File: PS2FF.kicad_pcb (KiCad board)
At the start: 2 copper layers, 38.1 x 74.7 mm, 11 parts, among them J1 PS2_SIDE, J2 DATA_RATE, J3 FF_SIDE, J4 POWER, SW1 DRIVE_TYPE, SW2 MEDIA_TYPE

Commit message: Fix up some DRC errors in the schematic
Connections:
- J3 pad 2: /~{FF_O_DENSITY} -> unconnected-(J3-Pad2)
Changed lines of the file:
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@@
   (net 22 "/DATA_RATE_0")
   (net 23 "/~{DISKETTE_CHANGE}")
-  (net 24 "/~{FF_O_DENSITY}")
+  (net 24 "unconnected-(J3-Pad2)")
   (net 25 "/~{FF_I_DS1}")
   (footprint "Connector_IDC:IDC-Header_2x17_P2.54mm_Horizontal" (layer "F.Cu")
@@
       (net 3 "GND") (pinfunction "Pin_1") (pintype "passive"))
     (pad "2" thru_hole circle (at 2.54 0) (size 1.7 1.7) (drill 1) (layers *.Cu *.Mask)
-      (net 24 "/~{FF_O_DENSITY}") (pinfunction "Pin_2") (pintype "passive+no_connect"))
+      (net 24 "unconnected-(J3-Pad2)") (pinfunction "Pin_2") (pintype "passive+no_connect"))
     (pad "3" thru_hole circle (at 0 -2.54) (size 1.7 1.7) (drill 1) (layers *.Cu *.Mask)
       (net 3 "GND") (pinfunction "Pin_3") (pintype "passive"))

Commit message: Bump the board rev since new changes
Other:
- board text added: "PS2FF Media Sense Adapter June Tate-Gans june@theonelab.com CC-BY-SA Board Rev B Schematic Rev B"
- board text removed: "PS2FF Media Sense Adapter June Tate-Gans june@theonelab.com CC-BY-SA Board Rev A Schematic Rev A"
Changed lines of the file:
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@@
     (effects (font (size 1 1) (thickness 0.15)) (justify left))
   )
-  (gr_text "PS2FF Media Sense Adapter\nJune Tate-Gans\njune@theonelab.com\nCC-BY-SA\nBoard Rev A\nSchematic Rev A" (at 110.998 60.833) (layer "F.SilkS")
+  (gr_text "PS2FF Media Sense Adapter\nJune Tate-Gans\njune@theonelab.com\nCC-BY-SA\nBoard Rev B\nSchematic Rev B" (at 110.998 60.833) (layer "F.SilkS")
     (effects (font (size 1 1) (thickness 0.15)) (justify left))
   )

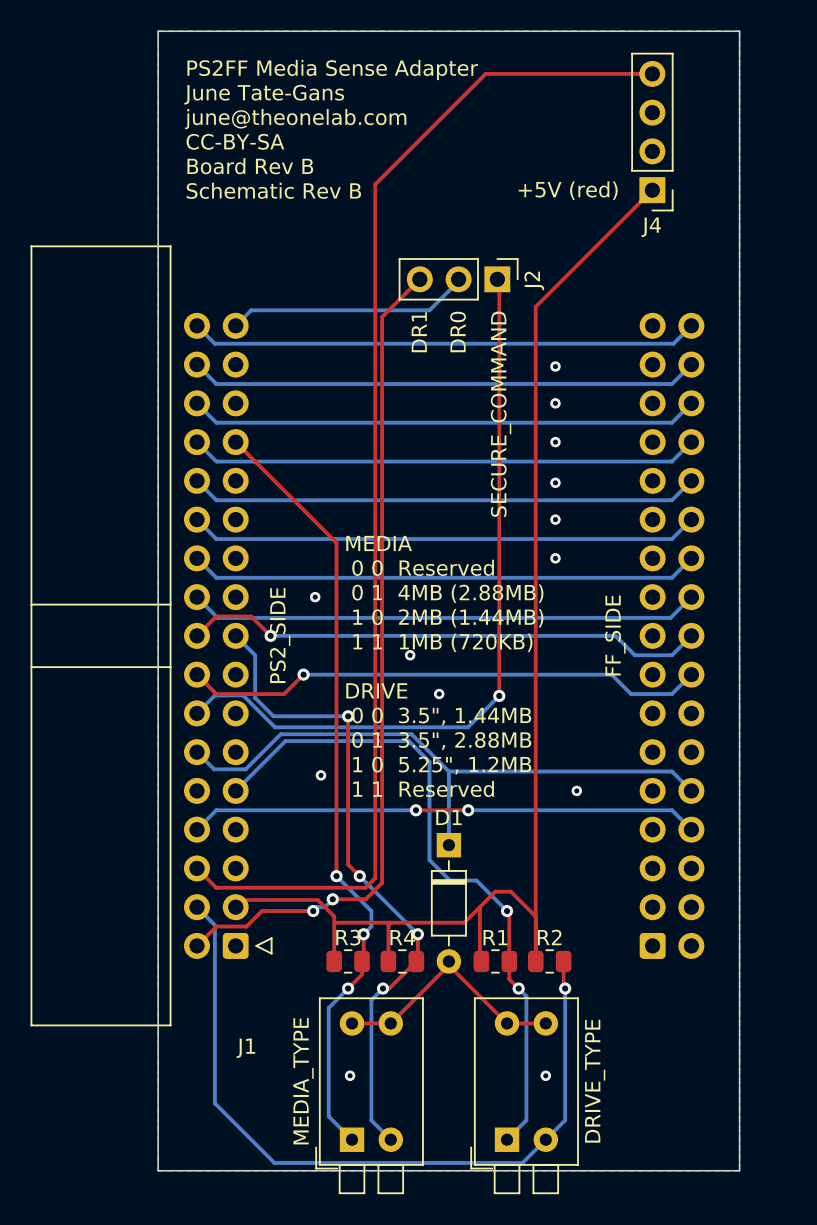
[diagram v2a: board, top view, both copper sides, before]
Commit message: automate things: Swap to using a buffer to automate
  - Use a simple buffer to drive outputs to the host side.
  - Wire in FF_O_DENSITY to the appropriate pin via the buffers.
    Note: this requires FF to be set to invert this output!
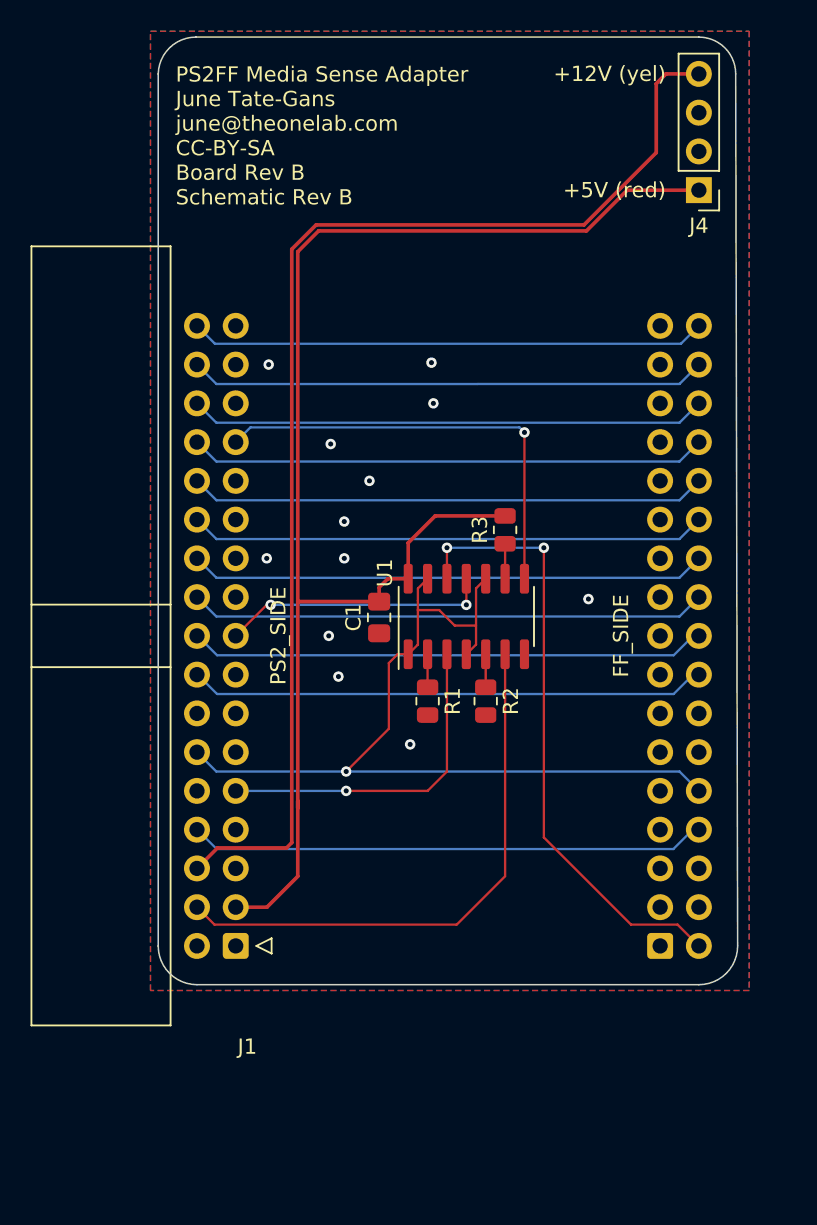
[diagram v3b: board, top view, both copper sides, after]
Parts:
- removed D1: 1N914, Diode_THT:D_DO-35_SOD27_P7.62mm_Horizontal
- removed J2: DATA_RATE, Connector_PinHeader_2.54mm:PinHeader_1x03_P2.54mm_Vertical
- removed R4: 1K, Resistor_SMD:R_0805_2012Metric
- removed SW1: DRIVE_TYPE, Button_Switch_THT:SW_DIP_SPSTx02_Piano_10.8x6.64mm_W7.62mm_P2.54mm
- removed SW2: MEDIA_TYPE, Button_Switch_THT:SW_DIP_SPSTx02_Piano_10.8x6.64mm_W7.62mm_P2.54mm
- added C1: 10pF, Capacitor_SMD:C_0805_2012Metric_Pad1.18x1.45mm_HandSolder, F.Cu at (123.7, 92.8)
- added U1: 74LS125, Package_SO:SOIC-14_3.9x8.7mm_P1.27mm, F.Cu at (129.4, 92.7)
- moved R3 30.1 mm to (132.0, 87.0), turned to 90 degrees
- moved R1 17.6 mm to (126.9, 98.3), turned to -90 degrees
- moved R2 17.6 mm to (130.7, 98.3), turned to -90 degrees
- moved J4 3.05 mm to (144.7, 64.8)
- moved J3 0.49 mm to (142.1, 114.3)
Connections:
- J3 pad 2: unconnected-(J3-Pad2) -> /~{FF_O_DENSITY}
- R1 pad 1: /DRIVE0_STATUS0 -> Net-(R1-Pad1)
- R1 pad 2: +5V -> GND
- R2 pad 1: /DRIVE1_STATUS1 -> Net-(R2-Pad1)
- R2 pad 2: +5V -> GND
- R3 pad 1: /MEDIA0_STATUS2 -> Net-(U1-Pad9)
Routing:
- net /DATA_RATE_1: track 54.4 -> 0.00 mm, vias 2 -> 0
- net /~{SECURITY_COMMAND}: track 49.4 -> 0.00 mm, vias 1 -> 0
- net /~{FF_O_DENSITY}: track 0.00 -> 40.5 mm, vias 0 -> 2
- net /MEDIA1_STATUS3: track 42.9 -> 17.7 mm, vias 4 -> 2
- net /MEDIA0_STATUS2: track 51.2 -> 29.0 mm, vias 3 -> 1
- net /DRIVE0_STATUS0: track 43.6 -> 22.1 mm, vias 2 -> 1
- net /~{DRIVE_SELECT}: track 40.2 -> 58.9 mm, vias 0 -> 1
- net Net-(D1-Pad2): track 16.1 -> 0.00 mm
- net /DATA_RATE_0: track 15.9 -> 0.00 mm
- net /DRIVE1_STATUS1: track 49.5 -> 36.5 mm, vias 1 -> 0
- net +5V: track 87.5 -> 92.2 mm
- net Net-(U1-Pad9): track 0.00 -> 2.29 mm
- net Net-(R2-Pad1): track 0.00 -> 2.16 mm
- net Net-(R1-Pad1): track 0.00 -> 2.16 mm
- net /~{FF_I_MO}: track 34.5 -> 33.4 mm, vias 1 -> 0
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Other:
- board size 38.1 x 74.7 mm -> 38 x 62.1 mm
- board text added: "+12V (yel)"
- board text removed: "DR0"
- board text removed: "DR1"
- board text removed: "MEDIA 0 0 Reserved 0 1 4MB (2.88MB) 1 0 2MB (1.44MB) 1 1 1MB (720KB) DRIVE 0 0 3.5{dblquote}, 1.44MB 0 1 3.5{dblquote}, 2.88MB 1 0 5.25{dblquote}, 1.2MB 1 1 Reserved"
- board text removed: "SECURE_COMMAND"

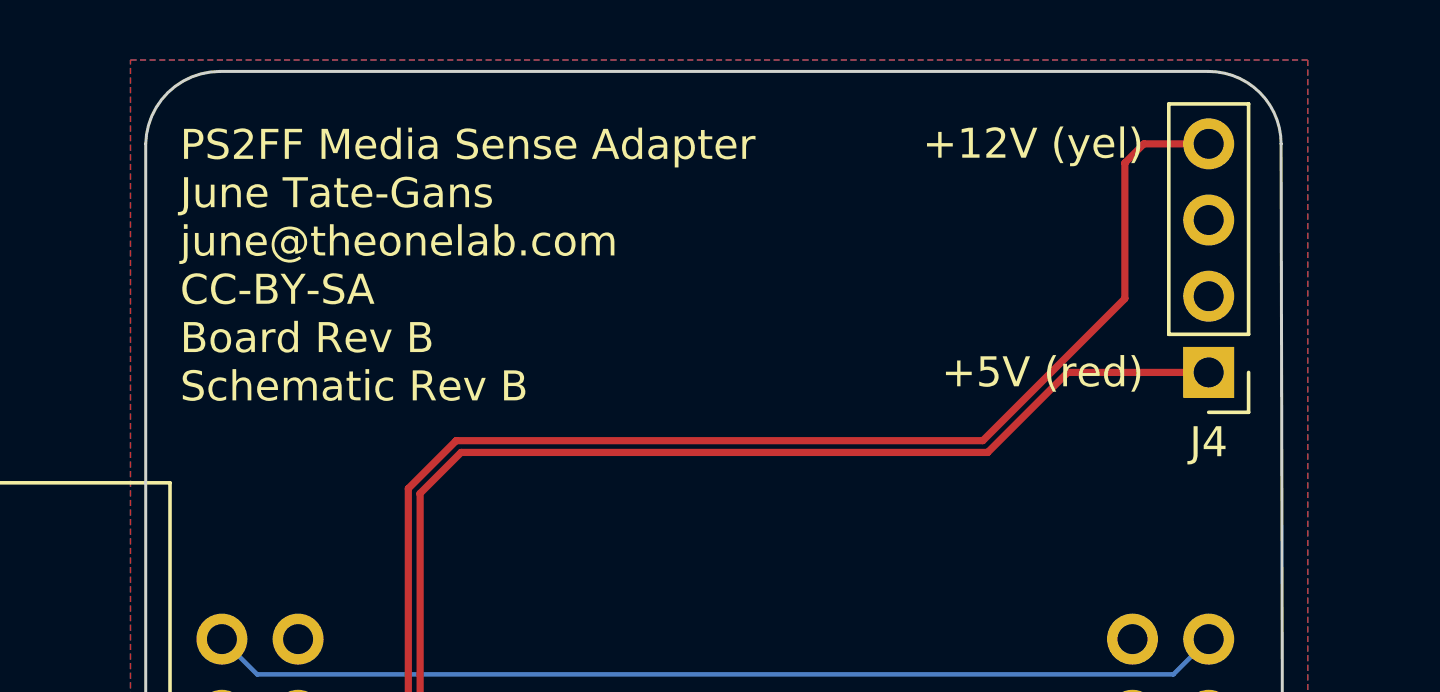
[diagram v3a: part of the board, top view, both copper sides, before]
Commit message: silks: Add a note about the hdout pin
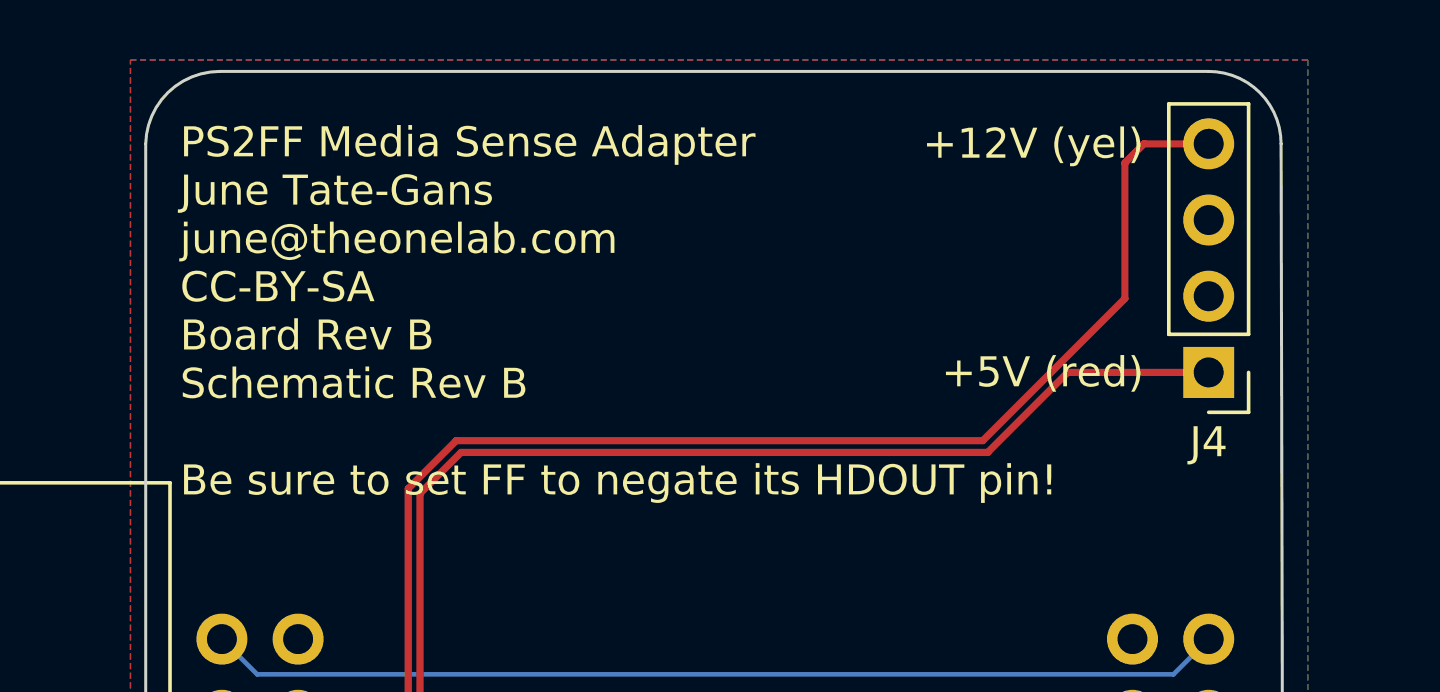
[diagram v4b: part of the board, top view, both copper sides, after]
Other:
- board text added: "PS2FF Media Sense Adapter June Tate-Gans june@theonelab.com CC-BY-SA Board Rev B Schematic Rev B Be sure to set FF to negate its HDOUT pin!"
- board text removed: "PS2FF Media Sense Adapter June Tate-Gans june@theonelab.com CC-BY-SA Board Rev B Schematic Rev B"
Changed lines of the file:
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@@
     (effects (font (size 1 1) (thickness 0.15)) (justify right))
   )
-  (gr_text "PS2FF Media Sense Adapter\nJune Tate-Gans\njune@theonelab.com\nCC-BY-SA\nBoard Rev B\nSchematic Rev B" (at 110.363 61.214) (layer "F.SilkS")
+  (gr_text "PS2FF Media Sense Adapter\nJune Tate-Gans\njune@theonelab.com\nCC-BY-SA\nBoard Rev B\nSchematic Rev B\n\nBe sure to set FF to negate its HDOUT pin!" (at 110.363 62.738) (layer "F.SilkS")
     (effects (font (size 1 1) (thickness 0.15)) (justify left))
   )

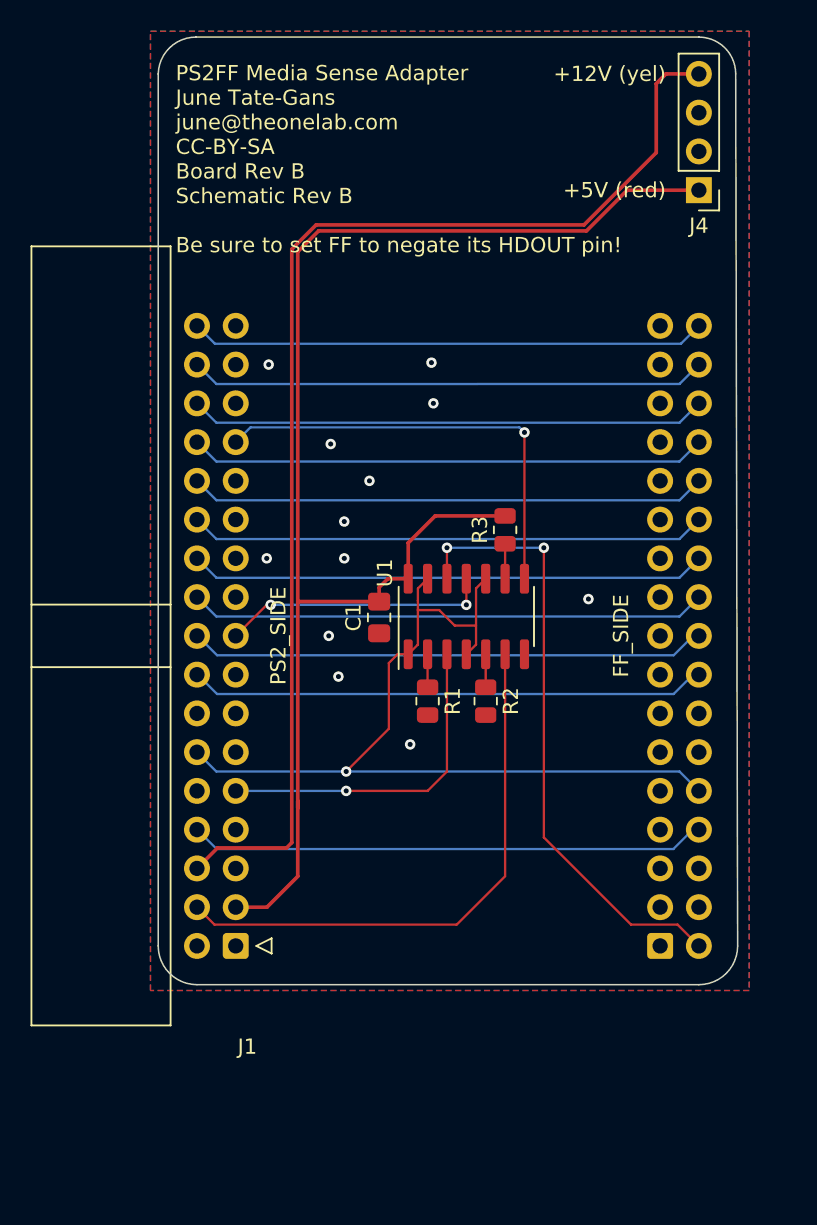
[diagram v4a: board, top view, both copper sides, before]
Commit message: writing: Actually wire up the HDOUT pin from the FF side
Update the links with the rev B schematic/PCB for fab.
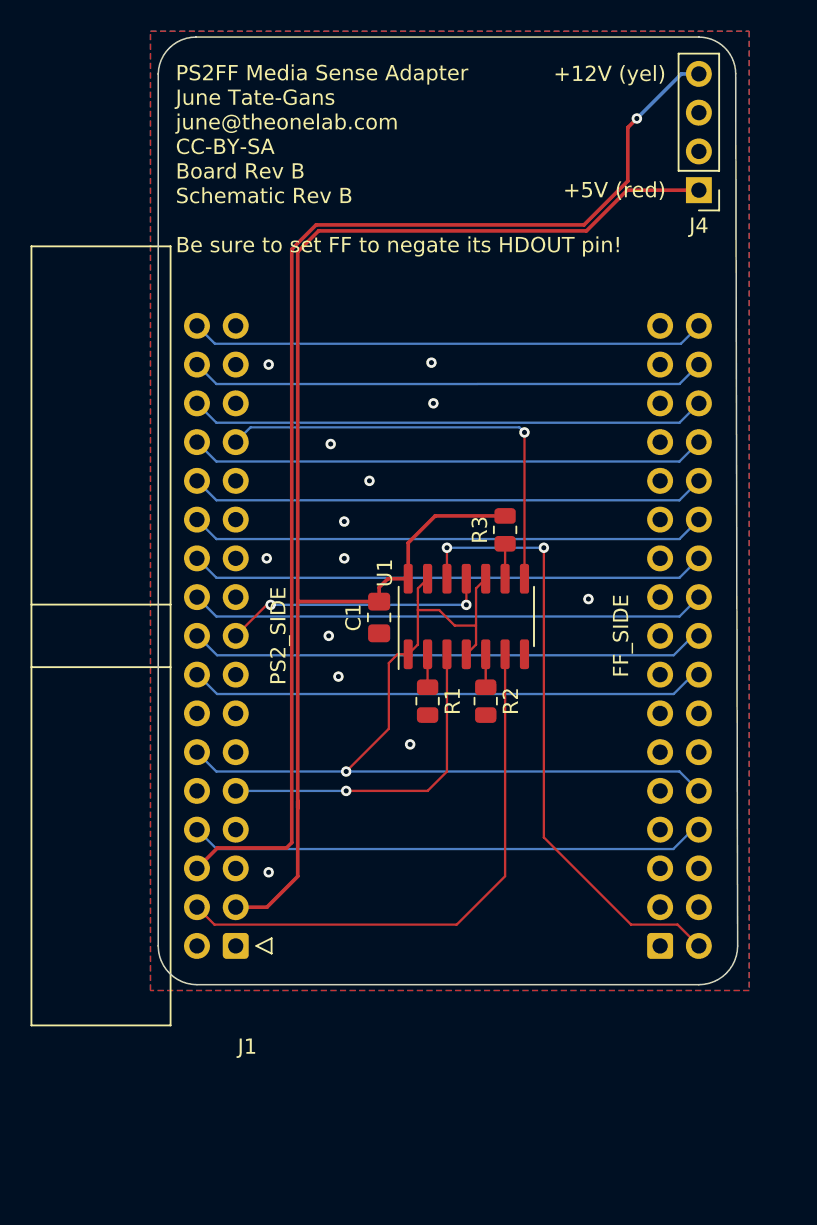
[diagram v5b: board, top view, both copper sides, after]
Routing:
- net +12V: track 79.9 -> 79.3 mm, vias 0 -> 1
- net GND: vias 12 -> 13
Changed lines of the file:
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@@
   (segment (start 121.539 102.87) (end 113.03 102.87) (width 0.1524) (layer "B.Cu") (net 1))
   (segment (start 113.03 102.87) (end 111.76 101.6) (width 0.1524) (layer "B.Cu") (net 1))
+  (via (at 116.459 109.474) (size 0.6858) (drill 0.3302) (layers "F.Cu" "B.Cu") (free) (net 2))
   (via (at 123.063 83.82) (size 0.6858) (drill 0.3302) (layers "F.Cu" "B.Cu") (free) (net 2))
   (via (at 127.254 78.74) (size 0.6858) (drill 0.3302) (layers "F.Cu" "B.Cu") (free) (net 2))
@@
   (segment (start 131.953 95.185) (end 131.953 109.728) (width 0.1524) (layer "F.Cu") (net 5))
   (segment (start 128.778 112.903) (end 112.903 112.903) (width 0.1524) (layer "F.Cu") (net 5))
-  (segment (start 113.103292 107.876708) (end 117.628354 107.876708) (width 0.24) (layer "F.Cu") (net 6))
-  (segment (start 117.9716 68.642715) (end 119.569715 67.0446) (width 0.24) (layer "F.Cu") (net 6))
-  (segment (start 117.628354 107.876708) (end 117.9716 107.533462) (width 0.24) (layer "F.Cu") (net 6))
-  (segment (start 111.76 109.22) (end 113.103292 107.876708) (width 0.24) (layer "F.Cu") (net 6))
-  (segment (start 142.494 57.15) (end 144.653 57.15) (width 0.24) (layer "F.Cu") (net 6))
-  (segment (start 141.859 62.310062) (end 141.859 57.785) (width 0.24) (layer "F.Cu") (net 6))
-  (segment (start 137.124462 67.0446) (end 141.859 62.310062) (width 0.24) (layer "F.Cu") (net 6))
-  (segment (start 119.569715 67.0446) (end 137.124462 67.0446) (width 0.24) (layer "F.Cu") (net 6))
-  (segment (start 117.9716 107.533462) (end 117.9716 68.642715) (width 0.24) (layer "F.Cu") (net 6))
-  (segment (start 141.859 57.785) (end 142.494 57.15) (width 0.24) (layer "F.Cu") (net 6))
+  (segment (start 117.9716 107.533462) (end 117.628354 107.876708) (width 0.24) (layer "F.Cu") (net 6))
+  (segment (start 117.9716 68.642715) (end 117.9716 107.533462) (width 0.24) (layer "F.Cu") (net 6))
+  (segment (start 113.103292 107.876708) (end 111.76 109.22) (width 0.24) (layer "F.Cu") (net 6))
+  (segment (start 137.124462 67.0446) (end 119.569715 67.0446) (width 0.24) (layer "F.Cu") (net 6))
+  (segment (start 139.995272 64.17379) (end 137.124462 67.0446) (width 0.24) (layer "F.Cu") (net 6))
+  (segment (start 140.589 60.071) (end 139.995272 60.664728) (width 0.24) (layer "F.Cu") (net 6))
+  (segment (start 119.569715 67.0446) (end 117.9716 68.642715) (width 0.24) (layer "F.Cu") (net 6))
+  (segment (start 117.628354 107.876708) (end 113.103292 107.876708) (width 0.24) (layer "F.Cu") (net 6))
+  (segment (start 139.995272 60.664728) (end 139.995272 64.17379) (width 0.24) (layer "F.Cu") (net 6))
+  (via (at 140.589 60.071) (size 0.6858) (drill 0.3302) (layers "F.Cu" "B.Cu") (net 6))
+  (segment (start 143.51 57.15) (end 144.653 57.15) (width 0.24) (layer "B.Cu") (net 6))
+  (segment (start 140.589 60.071) (end 143.51 57.15) (width 0.24) (layer "B.Cu") (net 6))
   (segment (start 113.05275 107.95) (end 142.97925 107.95) (width 0.1524) (layer "B.Cu") (net 7))
   (segment (start 142.97925 107.95) (end 144.21725 106.712) (width 0.1524) (layer "B.Cu") (net 7))
